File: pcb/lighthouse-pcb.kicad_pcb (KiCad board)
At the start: 2 copper layers, 45 x 45 mm, 47 parts, among them J1 USB_C_Receptacle_USB2.0, SW1 BOOT, SW3 ROOF, SW4 SW_DIP_x08, U1 ESP32-C3-WROOM-02, U2 CN5711, U3 AP2112K-3.3, U4 USBLC6-2SC6

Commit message: REV A release
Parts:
- removed C2: 220nf, Capacitor_SMD:C_0603_1608Metric
- removed REF**: SW_Push_1P1T_XKB_TS-1187A, lighthouse_footprints:SW_Push_1P1T_XKB_TS-1187A
- added H4: MountingHole M2.5, lighthouse_footprints:MountingHole_2.7mm_M2.5, F.Cu at (118.0, 82.5)
- added R12: 10k, Resistor_SMD:R_0603_1608Metric, F.Cu at (142.0, 57.4)
- added R13: 10k, Resistor_SMD:R_0603_1608Metric, F.Cu at (142.0, 89.0)
- added TP4: IO8, TestPoint:TestPoint_Pad_D1.0mm, F.Cu at (111.8, 65.8)
- added TP5: GND, TestPoint:TestPoint_Pad_D1.0mm, F.Cu at (105.5, 53.9)
- added TP6: 5V, TestPoint:TestPoint_Pad_D1.0mm, F.Cu at (114.6, 81.0)
- SW1: value BOOT -> BOOT/ROOF; footprint lighthouse_footprints:SW_SPST_PTS810 -> lighthouse_footprints:SW_Push_1P1T_XKB_TS-1187A
- SW3: value ROOF -> FRONT; footprint lighthouse_footprints:SW_SPST_PTS810 -> lighthouse_footprints:SW_Push_1P1T-MP_NO_Horizontal_Alps_SKRTLAE010
- moved H1 41.0 mm to (102.0, 51.7)
- moved R3 31.9 mm to (142.0, 55.8), turned to 180 degrees
- moved SW3 25.9 mm to (140.0, 51.7), turned to 180 degrees
- moved R1 10.7 mm to (111.5, 63.3), turned to -90 degrees
- moved C3 7.92 mm to (110.8, 59.0), turned to -90 degrees
- moved TP3 7.66 mm to (105.5, 55.3)
- moved R2 5.25 mm to (108.0, 56.1)
- moved H2 4.02 mm to (142.8, 93.8)
- moved C1 3.85 mm to (103.0, 56.1), turned to 0 degrees
- moved SW4 3.00 mm to (125.5, 76.9)
- moved C10 2.23 mm to (118.5, 86.1), turned to 180 degrees
- moved H3 2.00 mm to (104.0, 92.0)
- moved SW1 1.00 mm to (115.0, 76.0)
- moved C4 0.22 mm to (113.3, 83.1)
- moved C5 0.20 mm to (113.3, 85.0)
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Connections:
- net Net-(U1-EN) renamed /EN
- D3 pad 4: RX -> GPIO0
- SW3 pad 1: GPIO10 -> GND
- SW3 pad 2: GND -> GPIO2
- SW4 pad 1: TX -> GPIO10
- SW4 pad 2: GPIO3 -> RX/20
- SW4 pad 3: GPIO1 -> TX/21
- SW4 pad 4: GPIO0 -> GPIO3
- U1 pad 11: RX -> RX/20
- U1 pad 12: TX -> TX/21
- U2 pad 8: GPIO2 -> GPIO1
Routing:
- net GPIO2: track 79.2 -> 20.8 mm, vias 0 -> 2
- net +3V3: track 72.6 -> 97.1 mm, vias 3 -> 2
- net GPIO1: track 18.5 -> 42.8 mm, vias 2 -> 0
- net GPIO8: track 18.8 -> 4.96 mm
- net RX: track 12.0 -> 0.00 mm, vias 2 -> 0
- net GPIO3: track 14.3 -> 25.4 mm
- net TX: track 9.93 -> 0.00 mm
- net TX/21: track 0.00 -> 9.14 mm
- net RX/20: track 0.00 -> 7.10 mm
- net Net-(D2-DIN): track 44.2 -> 37.5 mm, vias 2 -> 4
- net GND: track 2.61 -> 7.36 mm, vias 27 -> 30
- net GPIO0: track 20.3 -> 16.5 mm, vias 2 -> 0
- net /EN: track 16.6 -> 12.8 mm
- net GPIO10: track 8.62 -> 5.22 mm
- net GPIO4: track 17.1 -> 19.1 mm
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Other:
- board text added: "2025.02 REV A"

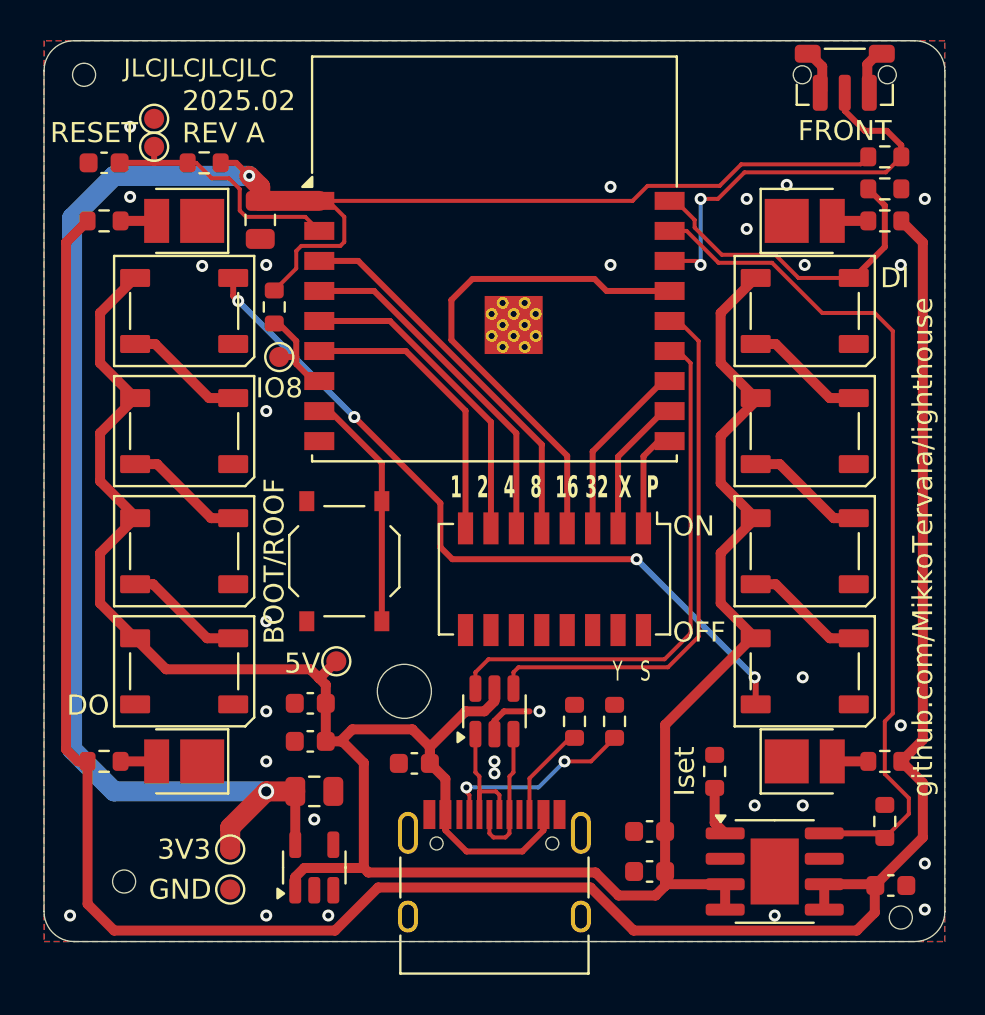
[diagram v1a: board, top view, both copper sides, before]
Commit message: Update GPIO0-2 schematic and layout
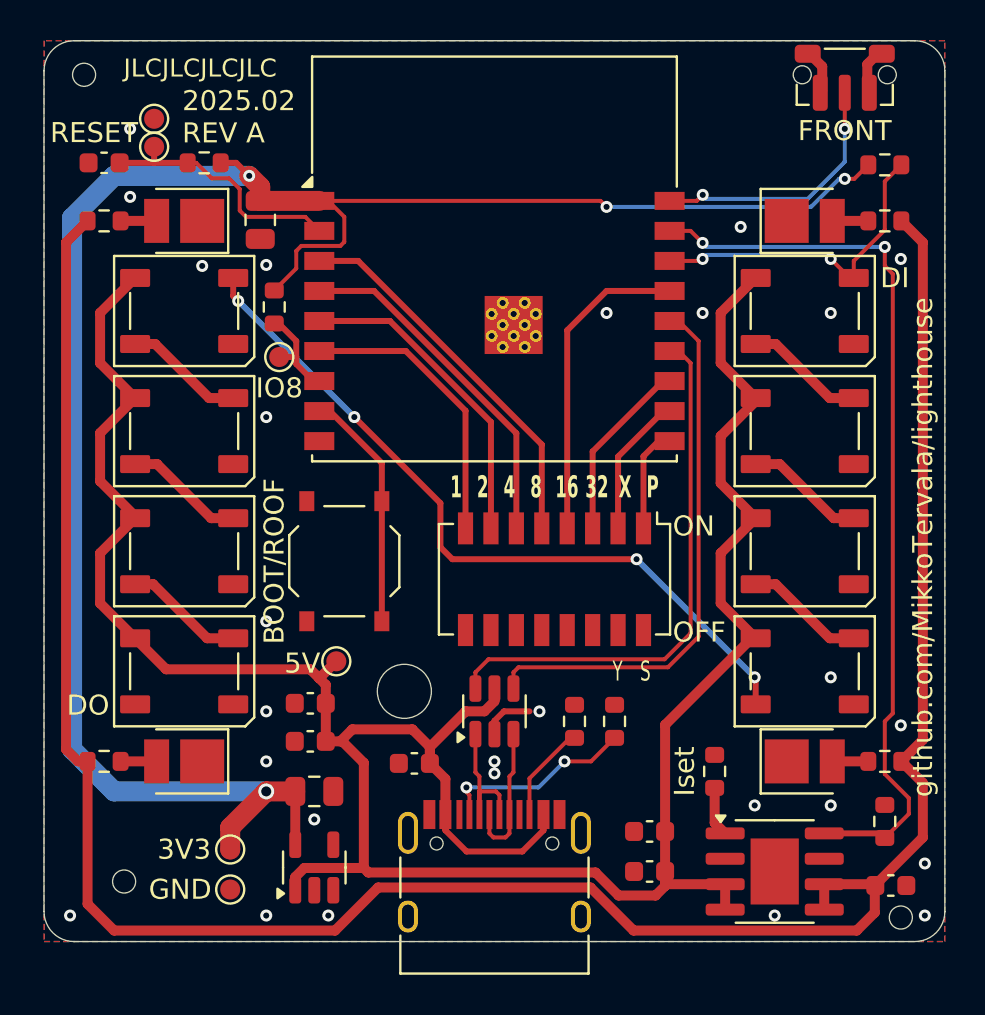
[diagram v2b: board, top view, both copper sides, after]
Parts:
- removed R12: 10k, Resistor_SMD:R_0603_1608Metric
- D10, D7, D8, D9: value LED 0.5W 2200k -> LED 0.5W 3000k
- R11: value ? -> 3k
- moved R3 0.40 mm to (142.0, 56.2)
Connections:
- D3 pad 4: GPIO0 -> GPIO2
- SW3 pad 2: GPIO2 -> GPIO0
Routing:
- net GPIO3: track 25.4 -> 15.8 mm
- net GPIO2: track 20.8 -> 16.4 mm
- net GPIO0: track 16.5 -> 13.2 mm, vias 0 -> 2
- net GPIO1: track 42.8 -> 45.1 mm, vias 0 -> 2
- net +3V3: track 97.1 -> 97.2 mm, vias 2 -> 4
- net GND: vias 30 -> 27

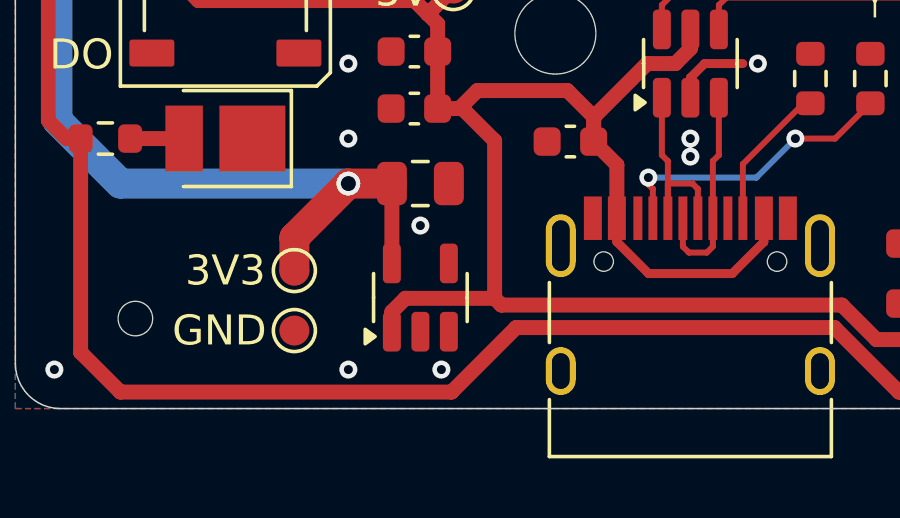
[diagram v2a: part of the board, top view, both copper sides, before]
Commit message: Added missing JLC part numbers and fixed U3 missing trace
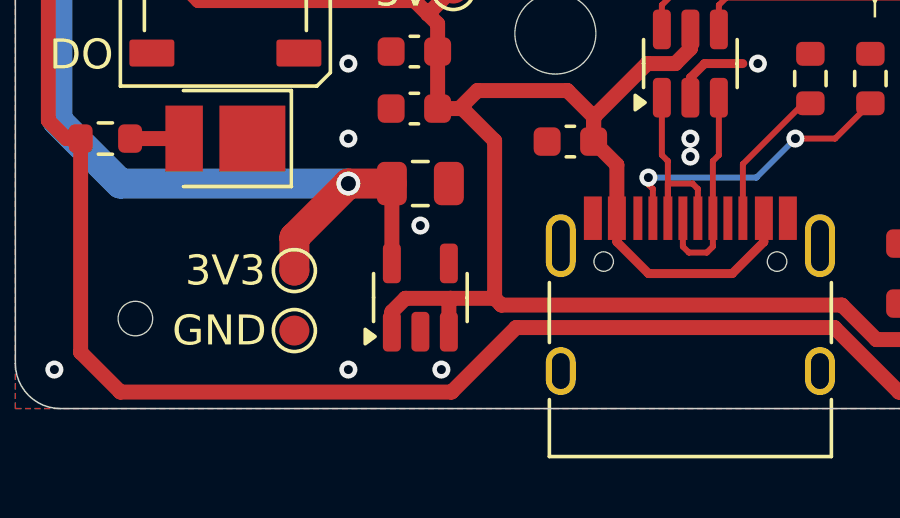
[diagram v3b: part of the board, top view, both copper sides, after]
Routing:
- net +5V: track 127.6 -> 128.7 mm
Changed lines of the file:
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@@
 		(sheetname "Root")
 		(sheetfile "lighthouse-pcb.kicad_sch")
-		(attr exclude_from_pos_files)
+		(attr exclude_from_pos_files exclude_from_bom)
 		(fp_circle
 			(center 0 0)
@@
 			)
 		)
+		(property "LCSC Part #" "C51118"
+			(at 0 0 90)
+			(unlocked yes)
+			(layer "F.Fab")
+			(hide yes)
+			(effects
+				(font
+					(size 1 1)
+					(thickness 0.15)
+				)
+			)
+		)
 		(property ki_fp_filters "SOT?23?5*")
 		(sheetname "Root")
@@
 		(sheetname "Root")
 		(sheetfile "lighthouse-pcb.kicad_sch")
-		(attr exclude_from_pos_files)
+		(attr exclude_from_pos_files exclude_from_bom)
 		(fp_circle
 			(center 0 0)
@@
 		(sheetname "Root")
 		(sheetfile "lighthouse-pcb.kicad_sch")
-		(attr exclude_from_pos_files)
+		(attr exclude_from_pos_files exclude_from_bom)
 		(fp_circle
 			(center 0 0)
@@
 		(sheetname "Root")
 		(sheetfile "lighthouse-pcb.kicad_sch")
-		(attr exclude_from_pos_files)
+		(attr exclude_from_pos_files exclude_from_bom)
 		(fp_circle
 			(center 0 0)
@@
 		(sheetname "Root")
 		(sheetfile "lighthouse-pcb.kicad_sch")
-		(attr exclude_from_pos_files)
+		(attr exclude_from_pos_files exclude_from_bom)
 		(fp_circle
 			(center 0 0)
@@
 		(sheetname "Root")
 		(sheetfile "lighthouse-pcb.kicad_sch")
-		(attr exclude_from_pos_files)
+		(attr exclude_from_pos_files exclude_from_bom)
 		(fp_circle
 			(center 0 0)
@@
 			)
 		)
+		(property "LCSC Part #" "C2934560"
+			(at 0 0 0)
+			(unlocked yes)
+			(layer "F.Fab")
+			(hide yes)
+			(effects
+				(font
+					(size 1 1)
+					(thickness 0.15)
+				)
+			)
+		)
 		(property ki_fp_filters "ESP32?C3*WROOM?02*")
 		(sheetname "Root")
@@
 	)
 	(gr_text "github.com/MikkoTervala/lighthouse"
-		(at 142.7 78.6 90)
+		(at 142.7 78.3 90)
 		(layer "B.SilkS")
 		(effects
@@
 	)
 	(segment
+		(start 114.45 92.4375)
+		(end 114.45 91.375)
+		(width 0.5)
+		(layer "F.Cu")
+		(net 3)
+	)
+	(segment
 		(start 112.55 91.775001)
 		(end 113.000001 91.325)
@@
 	)
 	(segment
+		(start 114.5 91.325)
+		(end 115.975 91.325)
+		(width 0.5)
+		(layer "F.Cu")
+		(net 3)
+	)
+	(segment
 		(start 133.8 69.755634)
 		(end 133.8 72.1)
@@
 	)
 	(segment
+		(start 114.45 91.375)
+		(end 114.5 91.325)
+		(width 0.5)
+		(layer "F.Cu")
+		(net 3)
+	)
+	(segment
 		(start 114.075 82.175)
 		(end 114.075 83)
@@
 	)
 	(segment
+		(start 113.000001 91.325)
+		(end 114.5 91.325)
+		(width 0.5)
+		(layer "F.Cu")
+		(net 3)
+	)
+	(segment
 		(start 131.025 91.5)
 		(end 131.025 92.135)
@@
 		(width 0.5)
 		(layer "F.Cu")
-		(net 3)
-	)
-	(segment
-		(start 113.000001 91.325)
-		(end 115.975 91.325)
-		(width 0.5)
-		(layer "F.Cu")

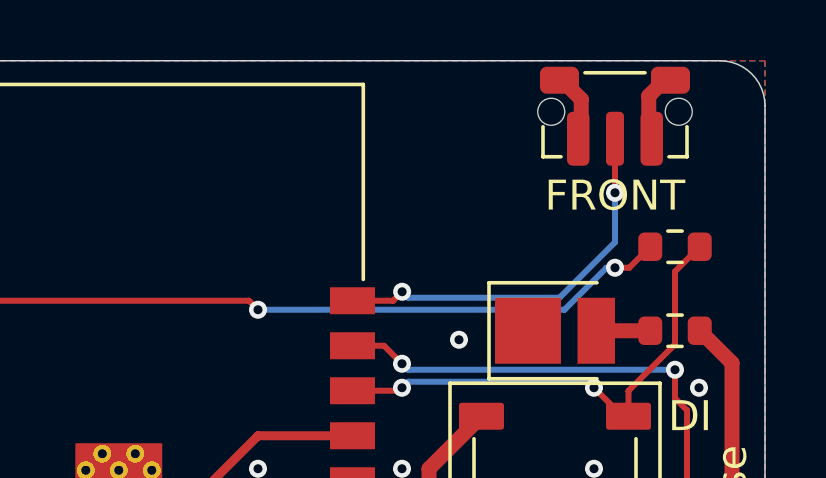
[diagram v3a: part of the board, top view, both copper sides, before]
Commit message: Add datamatrix location
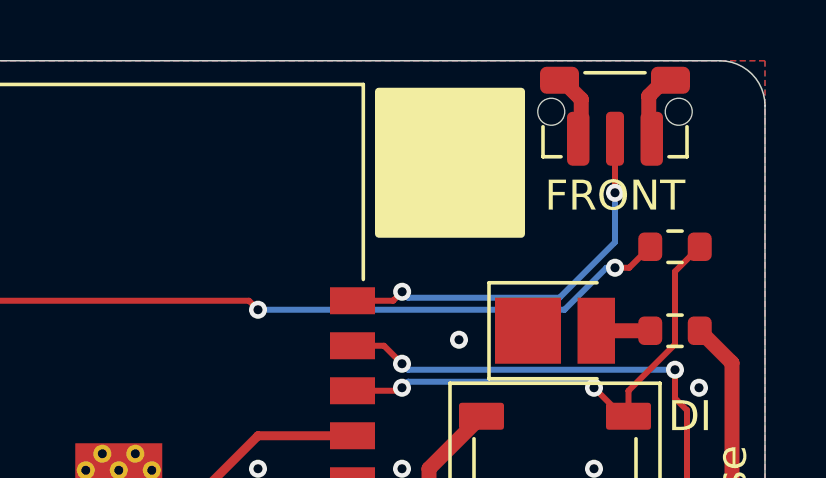
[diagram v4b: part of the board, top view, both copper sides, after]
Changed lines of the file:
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@@
+		)
+	)
+	(zone
+		(net 0)
+		(net_name "")
+		(layer "F.SilkS")
+		(hatch edge 0.5)
+		(connect_pads
+			(clearance 0)
+		)
+		(min_thickness 0.25)
+		(filled_areas_thickness no)
+		(fill yes
+			(thermal_gap 0.5)
+			(thermal_bridge_width 0.5)
+		)
+		(polygon
+			(pts
+				(xy 132 50.9) (xy 132 55.9) (xy 137 55.9) (xy 137 50.9)
+			)
 		)
 	)
